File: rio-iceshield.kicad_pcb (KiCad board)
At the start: 2 copper layers, 87.6 x 56 mm, 92 parts, among them J2 Conn_01x06, J3 Conn_01x06, J4 Conn_01x06, J5 Conn_01x06, J6 Conn_01x06, J7 Conn_02x06_Odd_Even, U1 ICE40UP5K-SG48ITR, U10 PC817, U11 PC817, U12 PC817, U13 PC817, U14 PC817, U2 AT25SF041B-SHD 4 Mb, U3 LD3985M122R_SOT23, U4 ULN2803A, U5 ULN2803A, U7 PC817, U8 PC817, U9 PC817, X2 XO91, j1 GPIO

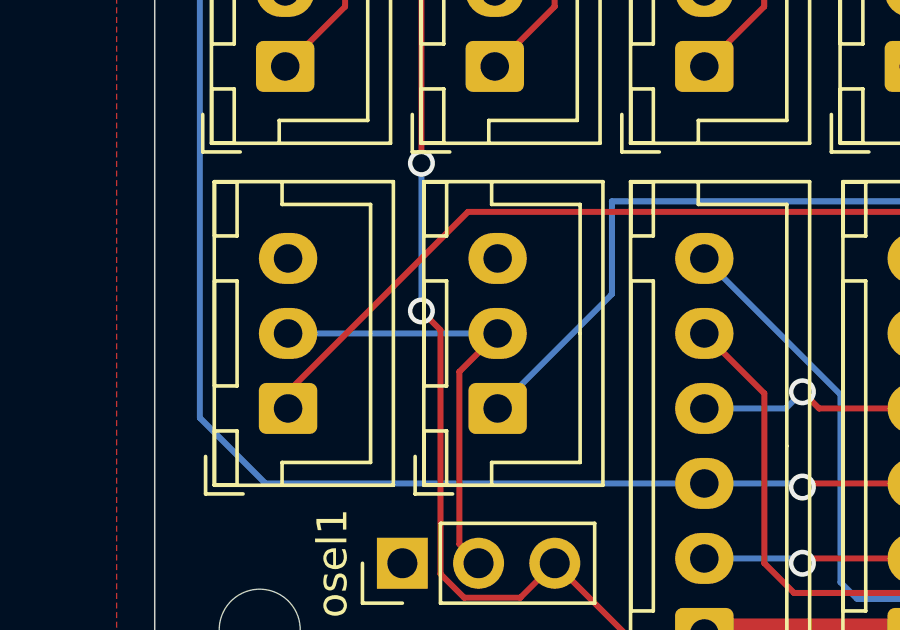
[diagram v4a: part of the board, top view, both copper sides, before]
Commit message: adding pullups to out1-2
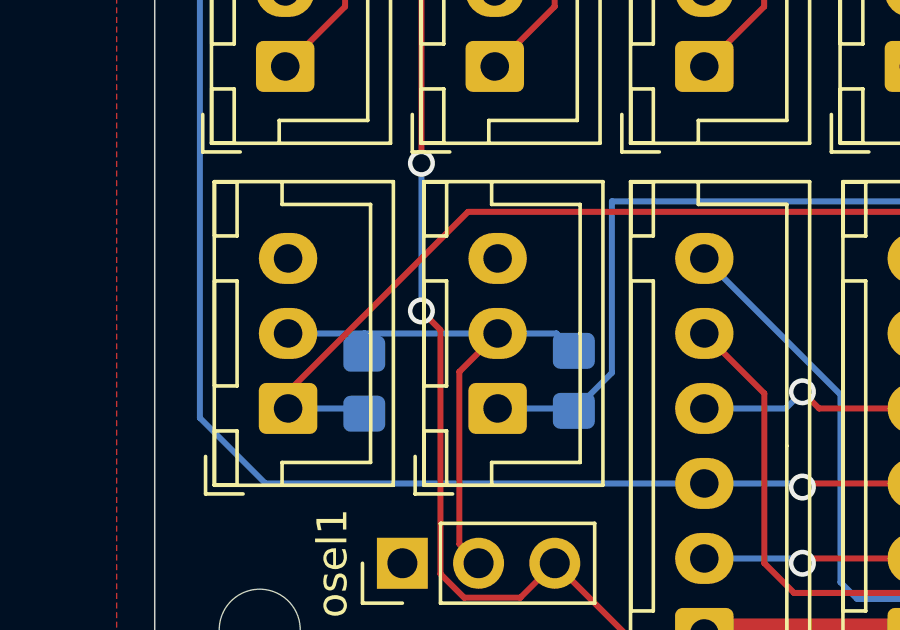
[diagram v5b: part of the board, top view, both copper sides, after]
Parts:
- added R31: 3k3, Resistor_SMD:R_0805_2012Metric_Pad1.20x1.40mm_HandSolder, B.Cu at (107.0, 88.3)
- added R32: 3k3, Resistor_SMD:R_0805_2012Metric_Pad1.20x1.40mm_HandSolder, B.Cu at (114.0, 88.2)
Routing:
- net out_power: track 15.4 -> 18.9 mm
- net out1: track 64.8 -> 67.4 mm
- net out2: track 60.5 -> 62.0 mm
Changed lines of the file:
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@@
+  )
+  (footprint "Resistor_SMD:R_0805_2012Metric_Pad1.20x1.40mm_HandSolder" (layer "B.Cu")
+    (at 106.985 88.3 90)
+    (descr "Resistor SMD 0805 (2012 Metric), square (rectangular) end terminal, IPC_7351 nominal with elongated pad for handsoldering. (Body size source: IPC-SM-782 page 72, https://www.pcb-3d.com/wordpress/wp-content/uploads/ipc-sm-782a_amendment_1_and_2.pdf), generated with kicad-footprint-generator")
+    (tags "resistor handsolder")
+    (property "Sheetfile" "rio-iceshield.kicad_sch")
+    (property "Sheetname" "")
+    (property "ki_description" "Resistor")
+    (property "ki_keywords" "R res resistor")
+    (attr smd)
+    (fp_text reference "R31" (at 0 1.65 90) (layer "B.SilkS")
+        (effects (font (size 1 1) (thickness 0.15)) (justify mirror))
+    )
+    (fp_text value "3k3" (at 0 -1.65 90) (layer "B.Fab")
+        (effects (font (size 1 1) (thickness 0.15)) (justify mirror))
+    )
+    (fp_text user "${REFERENCE}" (at 0 0 90) (layer "B.Fab")
+        (effects (font (size 0.5 0.5) (thickness 0.08)) (justify mirror))
+    )
+    (fp_line (start -0.227064 -0.735) (end 0.227064 -0.735)
+      (stroke (width 0.12) (type solid)) (layer "B.SilkS"))
+    (fp_line (start -0.227064 0.735) (end 0.227064 0.735)
+      (stroke (width 0.12) (type solid)) (layer "B.SilkS"))
+    (fp_line (start -1.85 -0.95) (end -1.85 0.95)
+      (stroke (width 0.05) (type solid)) (layer "B.CrtYd"))
+    (fp_line (start -1.85 0.95) (end 1.85 0.95)
+      (stroke (width 0.05) (type solid)) (layer "B.CrtYd"))
+    (fp_line (start 1.85 -0.95) (end -1.85 -0.95)
+      (stroke (width 0.05) (type solid)) (layer "B.CrtYd"))
+    (fp_line (start 1.85 0.95) (end 1.85 -0.95)
+      (stroke (width 0.05) (type solid)) (layer "B.CrtYd"))
+    (fp_line (start -1 -0.625) (end -1 0.625)
+      (stroke (width 0.1) (type solid)) (layer "B.Fab"))
+    (fp_line (start -1 0.625) (end 1 0.625)
+      (stroke (width 0.1) (type solid)) (layer "B.Fab"))
+    (fp_line (start 1 -0.625) (end -1 -0.625)
+      (stroke (width 0.1) (type solid)) (layer "B.Fab"))
+    (fp_line (start 1 0.625) (end 1 -0.625)
+      (stroke (width 0.1) (type solid)) (layer "B.Fab"))
+    (pad "1" smd roundrect (at -1 0 90) (size 1.2 1.4) (layers "B.Cu" "B.Paste" "B.Mask") (roundrect_rratio 0.208333)
+      (net 71 "out1") (pintype "passive"))
+    (pad "2" smd roundrect (at 1 0 90) (size 1.2 1.4) (layers "B.Cu" "B.Paste" "B.Mask") (roundrect_rratio 0.208333)
+      (net 39 "out_power") (pintype "passive"))
+    (model "${KICAD6_3DMODEL_DIR}/Resistor_SMD.3dshapes/R_0805_2012Metric.wrl"
+      (offset (xyz 0 0 0))
+      (scale (xyz 1 1 1))
+      (rotate (xyz 0 0 0))
+    )
   )
   (footprint "Resistor_SMD:R_0805_2012Metric_Pad1.20x1.40mm_HandSolder" (layer "B.Cu")
@@
       (net 12 "3v3") (pintype "passive"))
     (model "${KICAD6_3DMODEL_DIR}/Capacitor_SMD.3dshapes/C_0805_2012Metric.wrl"
+      (offset (xyz 0 0 0))
+      (scale (xyz 1 1 1))
+      (rotate (xyz 0 0 0))
+    )
+  )
+  (footprint "Resistor_SMD:R_0805_2012Metric_Pad1.20x1.40mm_HandSolder" (layer "B.Cu")
+    (at 113.97 88.205 90)
+    (descr "Resistor SMD 0805 (2012 Metric), square (rectangular) end terminal, IPC_7351 nominal with elongated pad for handsoldering. (Body size source: IPC-SM-782 page 72, https://www.pcb-3d.com/wordpress/wp-content/uploads/ipc-sm-782a_amendment_1_and_2.pdf), generated with kicad-footprint-generator")
+    (tags "resistor handsolder")
+    (property "Sheetfile" "rio-iceshield.kicad_sch")
+    (property "Sheetname" "")
+    (property "ki_description" "Resistor")
+    (property "ki_keywords" "R res resistor")
+    (attr smd)
+    (fp_text reference "R32" (at 0 1.65 90) (layer "B.SilkS")
+        (effects (font (size 1 1) (thickness 0.15)) (justify mirror))
+    )
+    (fp_text value "3k3" (at 0 -1.65 90) (layer "B.Fab")
+        (effects (font (size 1 1) (thickness 0.15)) (justify mirror))
+    )
+    (fp_text user "${REFERENCE}" (at 0 0 90) (layer "B.Fab")
+        (effects (font (size 0.5 0.5) (thickness 0.08)) (justify mirror))
+    )
+    (fp_line (start -0.227064 -0.735) (end 0.227064 -0.735)
+      (stroke (width 0.12) (type solid)) (layer "B.SilkS"))
+    (fp_line (start -0.227064 0.735) (end 0.227064 0.735)
+      (stroke (width 0.12) (type solid)) (layer "B.SilkS"))
+    (fp_line (start -1.85 -0.95) (end -1.85 0.95)
+      (stroke (width 0.05) (type solid)) (layer "B.CrtYd"))
+    (fp_line (start -1.85 0.95) (end 1.85 0.95)
+      (stroke (width 0.05) (type solid)) (layer "B.CrtYd"))
+    (fp_line (start 1.85 -0.95) (end -1.85 -0.95)
+      (stroke (width 0.05) (type solid)) (layer "B.CrtYd"))
+    (fp_line (start 1.85 0.95) (end 1.85 -0.95)
+      (stroke (width 0.05) (type solid)) (layer "B.CrtYd"))
+    (fp_line (start -1 -0.625) (end -1 0.625)
+      (stroke (width 0.1) (type solid)) (layer "B.Fab"))
+    (fp_line (start -1 0.625) (end 1 0.625)
+      (stroke (width 0.1) (type solid)) (layer "B.Fab"))
+    (fp_line (start 1 -0.625) (end -1 -0.625)
+      (stroke (width 0.1) (type solid)) (layer "B.Fab"))
+    (fp_line (start 1 0.625) (end 1 -0.625)
+      (stroke (width 0.1) (type solid)) (layer "B.Fab"))
+    (pad "1" smd roundrect (at -1 0 90) (size 1.2 1.4) (layers "B.Cu" "B.Paste" "B.Mask") (roundrect_rratio 0.208333)
+      (net 70 "out2") (pintype "passive"))
+    (pad "2" smd roundrect (at 1 0 90) (size 1.2 1.4) (layers "B.Cu" "B.Paste" "B.Mask") (roundrect_rratio 0.208333)
+      (net 39 "out_power") (pintype "passive"))
+    (model "${KICAD6_3DMODEL_DIR}/Resistor_SMD.3dshapes/R_0805_2012Metric.wrl"
       (offset (xyz 0 0 0))
       (scale (xyz 1 1 1))
@@
   (segment (start 110.155 93.645) (end 110.795 94.285) (width 0.2) (layer "F.Cu") (net 39))
   (segment (start 110.155 87.9) (end 110.155 93.645) (width 0.2) (layer "F.Cu") (net 39))
-  (segment (start 111.43 86.625) (end 104.445 86.625) (width 0.2) (layer "B.Cu") (net 39))
+  (segment (start 113.39 86.625) (end 111.43 86.625) (width 0.2) (layer "B.Cu") (net 39))
+  (segment (start 106.985 86.625) (end 104.445 86.625) (width 0.2) (layer "B.Cu") (net 39))
+  (segment (start 113.97 87.205) (end 113.39 86.625) (width 0.2) (layer "B.Cu") (net 39))
+  (segment (start 111.43 86.625) (end 106.985 86.625) (width 0.2) (layer "B.Cu") (net 39))
+  (segment (start 106.985 87.3) (end 106.985 86.625) (width 0.2) (layer "B.Cu") (net 39))
   (segment (start 127.3 75.73) (end 125.305 77.725) (width 0.2) (layer "F.Cu") (net 40))
   (segment (start 127.3 68.24) (end 127.3 75.73) (width 0.2) (layer "F.Cu") (net 40))
@@
   (segment (start 158.42 72.06) (end 157.15 73.33) (width 0.2) (layer "F.Cu") (net 70))
   (via (at 157.15 73.33) (size 0.9) (drill 0.6) (layers "F.Cu" "B.Cu") (net 70))
-  (segment (start 115.24 82.22) (end 115.24 85.315) (width 0.2) (layer "B.Cu") (net 70))
+  (segment (start 157.15 79.045) (end 153.975 82.22) (width 0.2) (layer "B.Cu") (net 70))
   (segment (start 157.15 73.33) (end 157.15 79.045) (width 0.2) (layer "B.Cu") (net 70))
-  (segment (start 157.15 79.045) (end 153.975 82.22) (width 0.2) (layer "B.Cu") (net 70))
-  (segment (start 115.24 85.315) (end 111.43 89.125) (width 0.2) (layer "B.Cu") (net 70))
+  (segment (start 114.05 89.125) (end 111.43 89.125) (width 0.2) (layer "B.Cu") (net 70))
+  (segment (start 115.24 82.22) (end 115.24 87.935) (width 0.2) (layer "B.Cu") (net 70))
   (segment (start 153.975 82.22) (end 115.24 82.22) (width 0.2) (layer "B.Cu") (net 70))
+  (segment (start 115.24 87.935) (end 114.05 89.125) (width 0.2) (layer "B.Cu") (net 70))
   (segment (start 157.15 79.114314) (end 153.692157 82.572157) (width 0.2) (layer "F.Cu") (net 71))
   (segment (start 104.445 88.57) (end 104.445 89.125) (width 0.2) (layer "F.Cu") (net 71))
@@
   (segment (start 153.692157 82.572157) (end 110.442843 82.572157) (width 0.2) (layer "F.Cu") (net 71))
   (segment (start 159.69 73.33) (end 158.42 73.33) (width 0.2) (layer "F.Cu") (net 71))
+  (segment (start 106.81 89.125) (end 106.985 89.3) (width 0.2) (layer "B.Cu") (net 71))
+  (segment (start 104.445 89.125) (end 106.81 89.125) (width 0.2) (layer "B.Cu") (net 71))
   (segment (start 173.025 79.68) (end 168.99 79.68) (width 0.2) (layer "F.Cu") (net 72))
   (segment (start 176.425 75.5625) (end 176.425 76.28) (width 0.2) (layer "F.Cu") (net 72))
